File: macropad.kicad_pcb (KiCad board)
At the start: 2 copper layers, 4 parts, among them SW1 SW_Push, SW2 SW_Push, SW3 SW_Push, U1 MOUDLE-SEEEDUINO-XIAO

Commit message: done w pcb, moving to fusioin
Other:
- board outline added: 57 x 40 mm
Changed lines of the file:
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@@
 		)
 		(property "Value" "SW_Push"
-			(at 59.804 -6.75347 0)
+			(at -2.5 13.08 0)
 			(layer "F.Fab")
 			(effects
@@
 		)
 	)
+	(gr_rect
+		(start 100.5 78)
+		(end 157.5 118)
+		(stroke
+			(width 0.05)
+			(type default)
+		)
+		(fill none)
+		(layer "Edge.Cuts")
+	)
+	(dimension
+		(type aligned)
+		(layer "Edge.Cuts")
+		(pts
+			(xy 100.475 118.025) (xy 157.5 118)
+		)
+		(height 6.153188)
+		(gr_text "57.0250 mm"
+			(at 128.989694 123.015687 0.02511870927)
+			(layer "Edge.Cuts")
+			(effects
+				(font
+					(size 1 1)
+					(thickness 0.15)
+				)
+			)
+		)
+		(format
+			(prefix "")
+			(suffix "")
+			(units 3)
+			(units_format 1)
+			(precision 4)
+		)
+		(style
+			(thickness 0.05)
+			(arrow_length 1.27)
+			(text_position_mode 0)
+			(extension_height 0.58642)
+			(extension_offset 0.5) keep_text_aligned)
+	)
+	(dimension
+		(type aligned)
+		(layer "Edge.Cuts")
+		(pts
+			(xy 157.5 78) (xy 157.485 118.025)
+		)
+		(height -4.679811)
+		(gr_text "40.0250 mm"
+			(at 161.022311 98.013823 89.9785275)
+			(layer "Edge.Cuts")
+			(effects
+				(font
+					(size 1 1)
+					(thickness 0.15)
+				)
+			)
+		)
+		(format
+			(prefix "")
+			(suffix "")
+			(units 3)
+			(units_format 1)
+			(precision 4)
+		)
+		(style
+			(thickness 0.05)
+			(arrow_length 1.27)
+			(text_position_mode 0)
+			(extension_height 0.58642)
+			(extension_offset 0.5) keep_text_aligned)
+	)
 	(segment

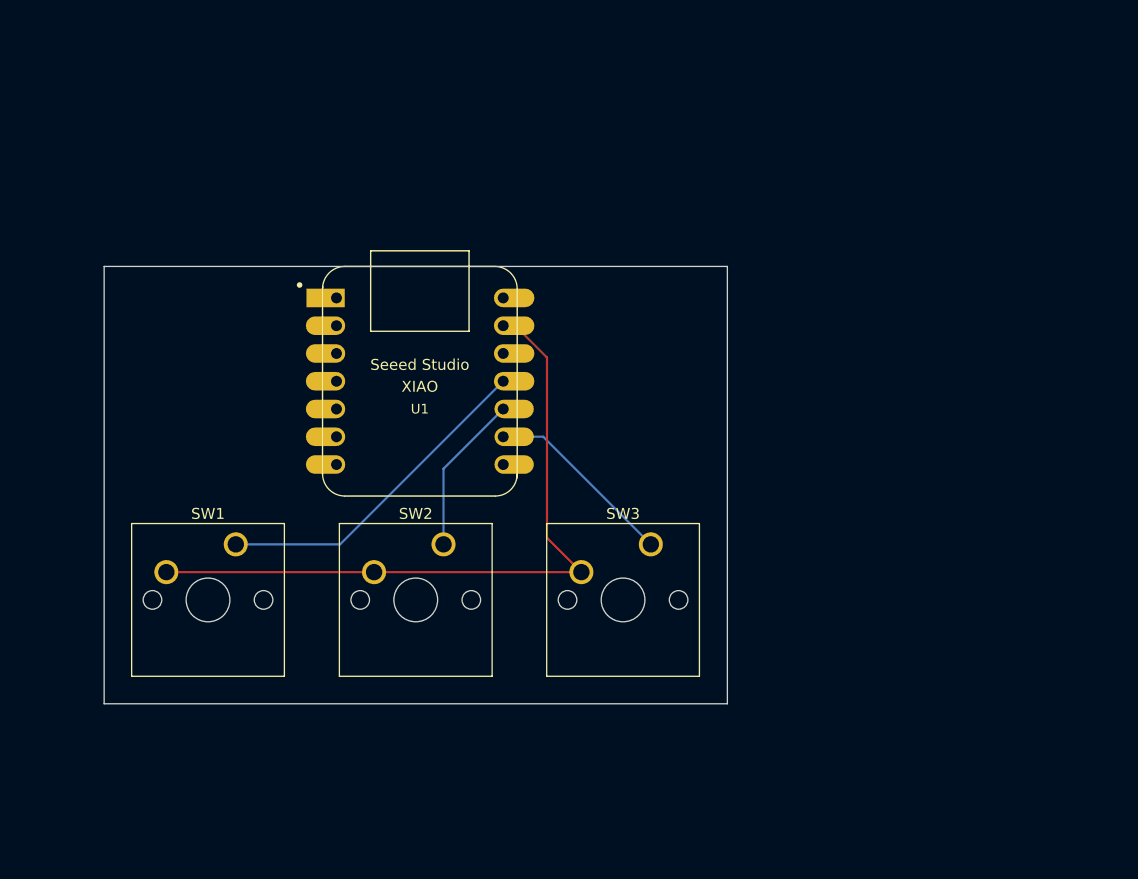
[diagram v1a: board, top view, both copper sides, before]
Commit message: need to fix errors
so far i have 3 keys, one rotary encoder, and an oled screen
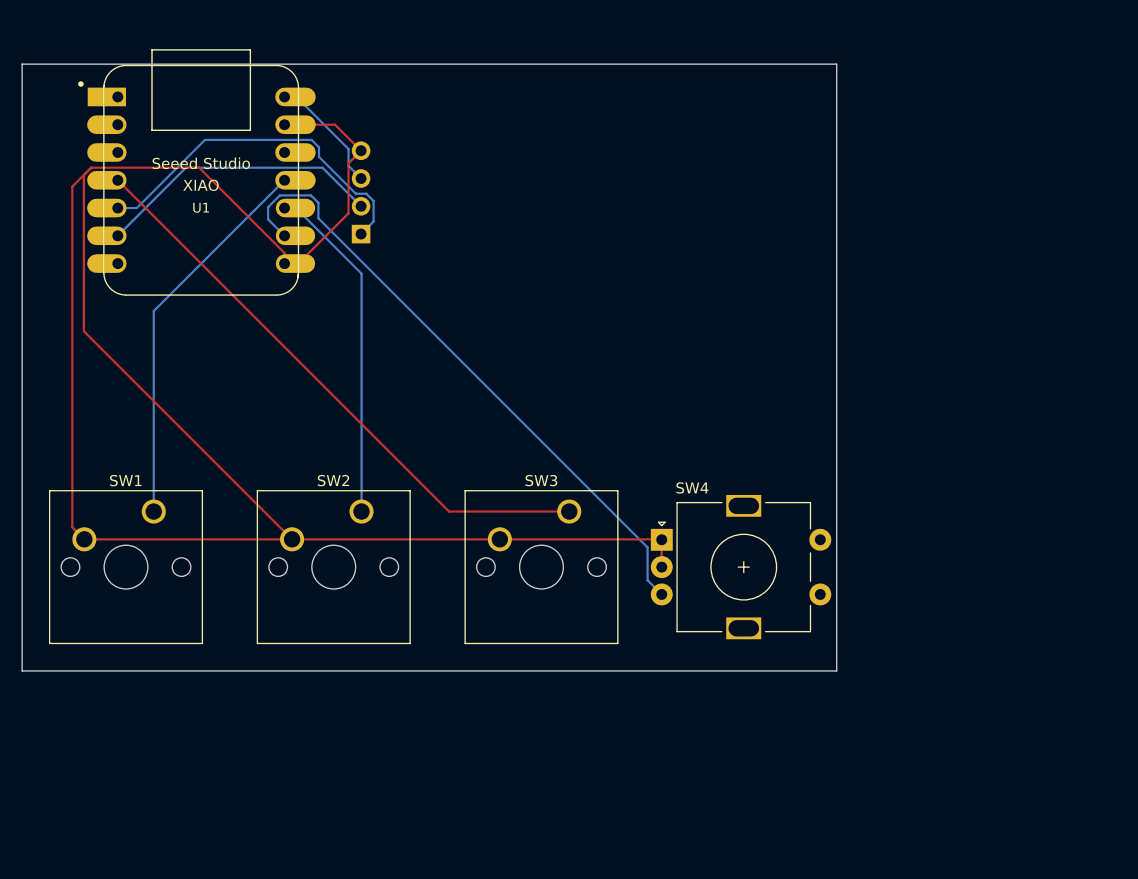
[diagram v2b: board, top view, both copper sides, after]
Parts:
- added J1: OLED_128x32, XIAO_PCB:OLED_128x32, F.Cu at (122.4, 65.2)
- added SW4: RotaryEncoder_Switch, Rotary_Encoder:RotaryEncoder_Alps_EC11E-Switch_Vertical_H20mm, F.Cu at (151.5, 103.0)
- moved U1 27.2 mm to (109.4, 70.1)
- moved SW1 8.08 mm to (105.0, 100.4)
- moved SW2 8.08 mm to (124.0, 100.4)
- moved SW3 8.04 mm to (143.0, 100.4)
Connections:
- SW1 pad 2: GND -> EC11A
- SW2 pad 2: GND -> EC11A
- SW3 pad 1: Net-(U1-PA7_A8_D8_SCK) -> Net-(U1-PA11_A3_D3)
- SW3 pad 2: GND -> EC11A
- U1 pad 13: GND -> EC11A
- U1 pad 4: unconnected-(U1-PA11_A3_D3-Pad4) -> Net-(U1-PA11_A3_D3)
- U1 pad 5: unconnected-(U1-PA8_A4_D4_SDA-Pad5) -> 5DA
- U1 pad 6: unconnected-(U1-PA9_A5_D5_SCL-Pad6) -> 5CL
- U1 pad 8: Net-(U1-PB09_A7_D7_RX) -> EC11A
- U1 pad 9: Net-(U1-PA7_A8_D8_SCK) -> EC11B
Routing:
- net EC11A: track 0.00 -> 176.5 mm
- net GND: track 64.1 -> 0.00 mm
- net EC11B: track 0.00 -> 57.4 mm
- net Net-(U1-PA11_A3_D3): track 0.00 -> 53.8 mm
- net 5DA: track 0.00 -> 32.3 mm
- net 5CL: track 0.00 -> 26.3 mm
- net Net-(U1-PA7_A8_D8_SCK): track 17.6 -> 0.00 mm
- net Net-(U1-PA5_A9_D9_MISO): track 14.6 -> 31.3 mm
- net VCC: track 0.00 -> 11.0 mm
- net Net-(U1-PA6_A10_D10_MOSI): track 30.6 -> 35.3 mm
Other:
- board size 57 x 40 mm -> 74.5 x 55.5 mm

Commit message: fixed wiring on sch
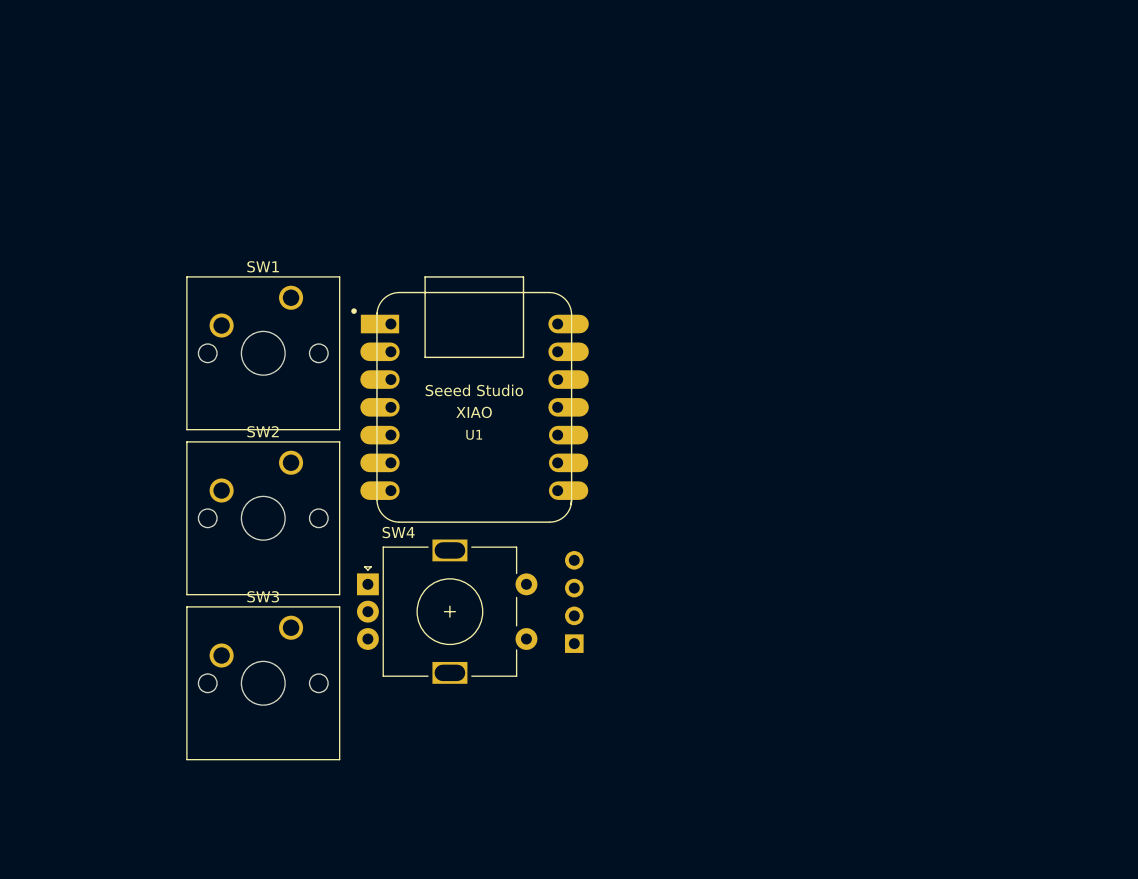
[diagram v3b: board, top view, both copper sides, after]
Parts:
- moved J1 42.2 mm to (141.9, 102.7)
- moved U1 32.5 mm to (134.4, 90.9)
- moved SW3 27.6 mm to (117.6, 111.0)
- moved SW4 27.2 mm to (124.6, 107.1)
- moved SW1 23.2 mm to (117.6, 80.9)
- moved SW2 7.84 mm to (117.6, 96.0)
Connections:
- J1 pad 1: 5DA -> GND
- J1 pad 2: 5CL -> +3.3V
- J1 pad 3: VCC -> Net-(J1-SCL)
- J1 pad 4: EC11A -> Net-(J1-SDA)
- SW1 pad 2: EC11A -> GND
- SW2 pad 2: EC11A -> GND
- SW3 pad 2: EC11A -> GND
- SW4 pad C: EC11A -> GND
- U1 pad 12: unconnected-(U1-3V3-Pad12) -> +3.3V
- U1 pad 13: EC11A -> GND
- U1 pad 14: VCC -> unconnected-(U1-5V-Pad14)
- U1 pad 5: 5DA -> Net-(J1-SDA)
- U1 pad 6: 5CL -> Net-(J1-SCL)
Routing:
- net EC11A: track 176.5 -> 0.00 mm
- net EC11B: track 57.4 -> 0.00 mm
- net Net-(U1-PA11_A3_D3): track 53.8 -> 0.00 mm
- net Net-(U1-PA6_A10_D10_MOSI): track 35.3 -> 0.00 mm
- net 5DA: track 32.3 -> 0.00 mm
- net Net-(U1-PA5_A9_D9_MISO): track 31.3 -> 0.00 mm
- net 5CL: track 26.3 -> 0.00 mm
- net VCC: track 11.0 -> 0.00 mm
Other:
- board outline removed

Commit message: final fixes on pcb + sch files
can't wait to start the model!
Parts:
- moved SW4 53.9 mm to (177.0, 120.0)
- moved SW3 51.3 mm to (168.5, 117.4)
- moved SW1 38.8 mm to (130.5, 117.4)
- moved SW2 38.5 mm to (149.5, 117.4)
- moved J1 18.6 mm to (152.4, 87.3)
- moved U1 7.36 mm to (138.9, 85.1)
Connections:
- SW4 pad S1: EC11SWB -> GND
- SW4 pad S2: EC11SWA -> Net-(U1-PA02_A0_D0)
- U1 pad 1: unconnected-(U1-PA02_A0_D0-Pad1) -> Net-(U1-PA02_A0_D0)
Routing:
- net GND: track 0.00 -> 116.5 mm
- net Net-(U1-PA02_A0_D0): track 0.00 -> 79.7 mm
- net Net-(U1-PA11_A3_D3): track 0.00 -> 58.9 mm
- net EC11A: track 0.00 -> 54.2 mm
- net EC11B: track 0.00 -> 51.9 mm
- net Net-(U1-PA6_A10_D10_MOSI): track 0.00 -> 39.0 mm
- net Net-(U1-PA5_A9_D9_MISO): track 0.00 -> 32.0 mm
- net +3.3V: track 0.00 -> 26.2 mm
- net Net-(J1-SCL): track 0.00 -> 23.5 mm
- net Net-(J1-SDA): track 0.00 -> 23.5 mm
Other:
- board outline added: 74.5 x 57.5 mm

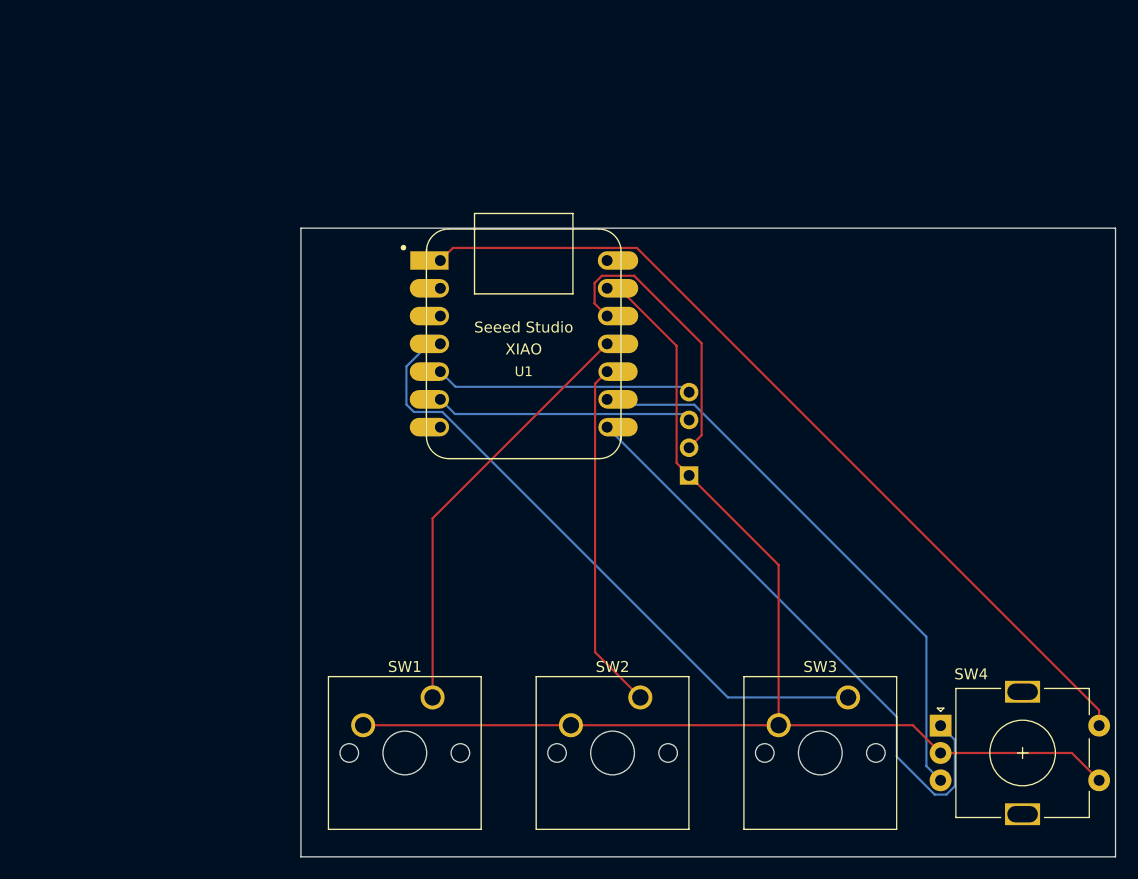
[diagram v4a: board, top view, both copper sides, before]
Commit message: change pcb size to fit sushi cat
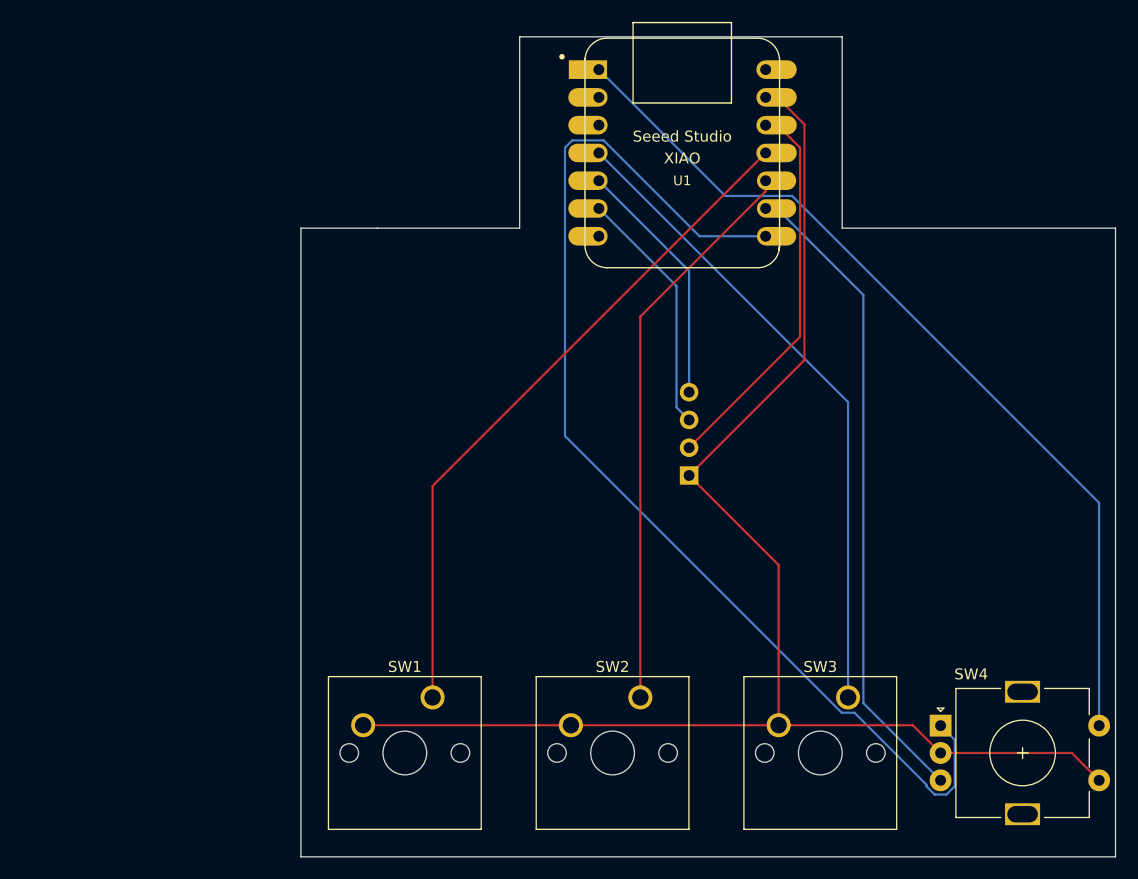
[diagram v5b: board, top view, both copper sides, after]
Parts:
- moved U1 22.7 mm to (153.4, 67.6)
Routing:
- net EC11A: track 54.2 -> 104.3 mm
- net Net-(U1-PA6_A10_D10_MOSI): track 39.0 -> 62.4 mm
- net GND: track 116.5 -> 136.7 mm
- net Net-(U1-PA5_A9_D9_MISO): track 32.0 -> 52.0 mm
- net +3.3V: track 26.2 -> 35.6 mm
- net EC11B: track 51.9 -> 59.5 mm
- net Net-(U1-PA02_A0_D0): track 79.7 -> 82.5 mm
- net Net-(J1-SCL): track 23.5 -> 22.8 mm
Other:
- board size 74.5 x 57.5 mm -> 74.5 x 75 mm
